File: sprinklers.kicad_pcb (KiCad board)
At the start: 2 copper layers, 128.7 x 88 mm, 43 parts, among them K1 SANYOU_SRD_Form_C, K2 SANYOU_SRD_Form_C, K3 SANYOU_SRD_Form_C, K4 SANYOU_SRD_Form_C, K5 SANYOU_SRD_Form_C, K6 SANYOU_SRD_Form_C, Q1 Q_NMOS_GDS, Q2 Q_NMOS_GDS, Q3 Q_NMOS_GDS, Q4 Q_NMOS_GDS, Q5 Q_NMOS_GDS, Q6 Q_NMOS_GDS, U1 LM2596S-5, U2 ESP32-WROOM-32D, U3 AP1117-33

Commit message: orgenize schematic
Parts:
- added 26 27 28 29: PinHeader_1x04_P2.54mm_Vertical, Connector_PinHeader_2.54mm:PinHeader_1x04_P2.54mm_Vertical, F.Cu at (145.0, 56.9)
- GND 5V 3V3: renamed from DC OUT
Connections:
- C5 pad 1: AC -> Net-(D4-K)
- D4 pad 1: AC -> Net-(D4-K)
- U1 pad 1: AC -> Net-(D4-K)
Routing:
- net AC: track 165.7 -> 127.0 mm
- net Net-(D4-K): track 0.00 -> 38.0 mm
- net unconnected-(U2-IO5-Pad29): track 0.00 -> 7.18 mm
- net unconnected-(U2-IO17-Pad28): track 0.00 -> 6.66 mm
- net unconnected-(U2-IO4-Pad26): track 0.00 -> 6.52 mm
- net unconnected-(U2-IO16-Pad27): track 0.00 -> 6.13 mm
- net unconnected-(U2-IO0-Pad25): track 30.5 -> 33.2 mm
- net unconnected-(U2-TXD0/IO1-Pad35): track 11.8 -> 9.62 mm
- net Net-(U1-FB): track 202.3 -> 203.0 mm, vias 4 -> 3
- net unconnected-(U2-EN-Pad3): track 36.6 -> 36.0 mm

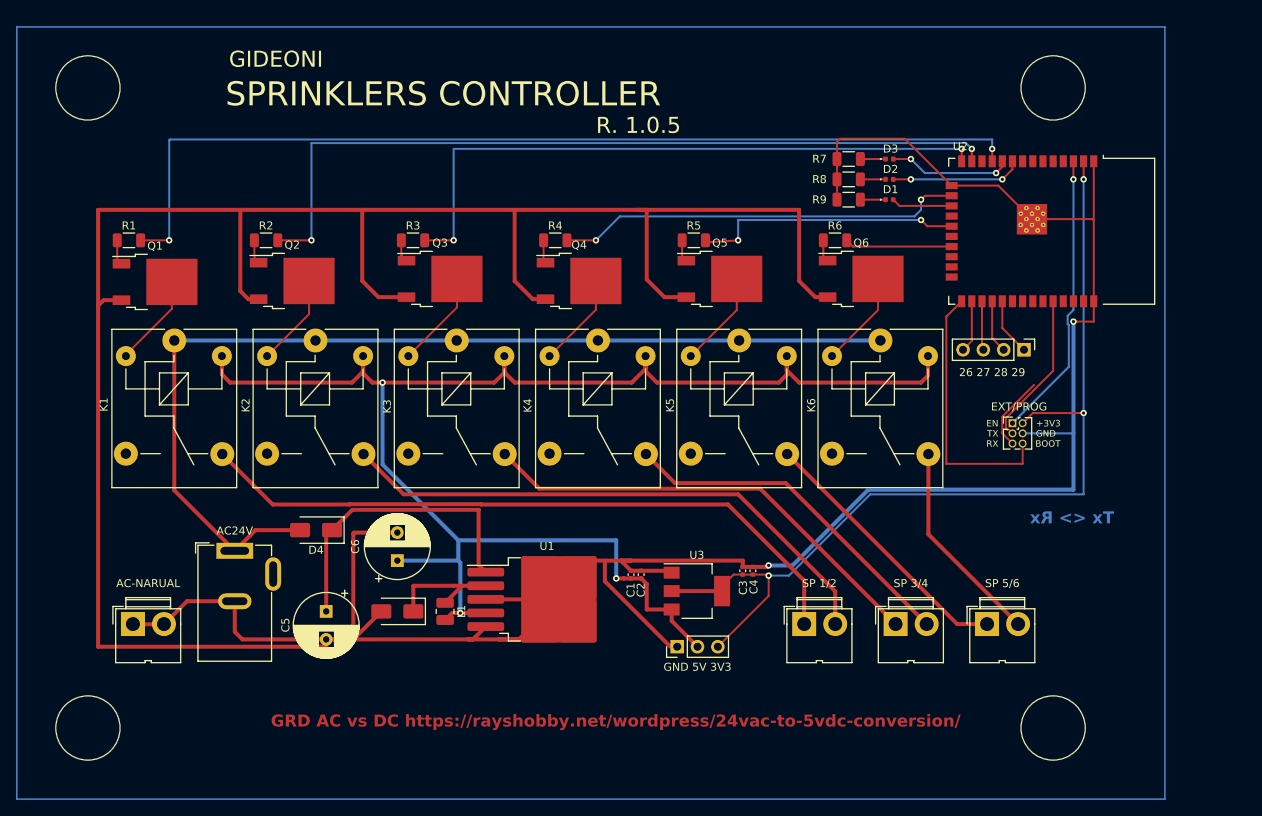
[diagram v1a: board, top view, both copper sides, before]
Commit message: Replacing inductor
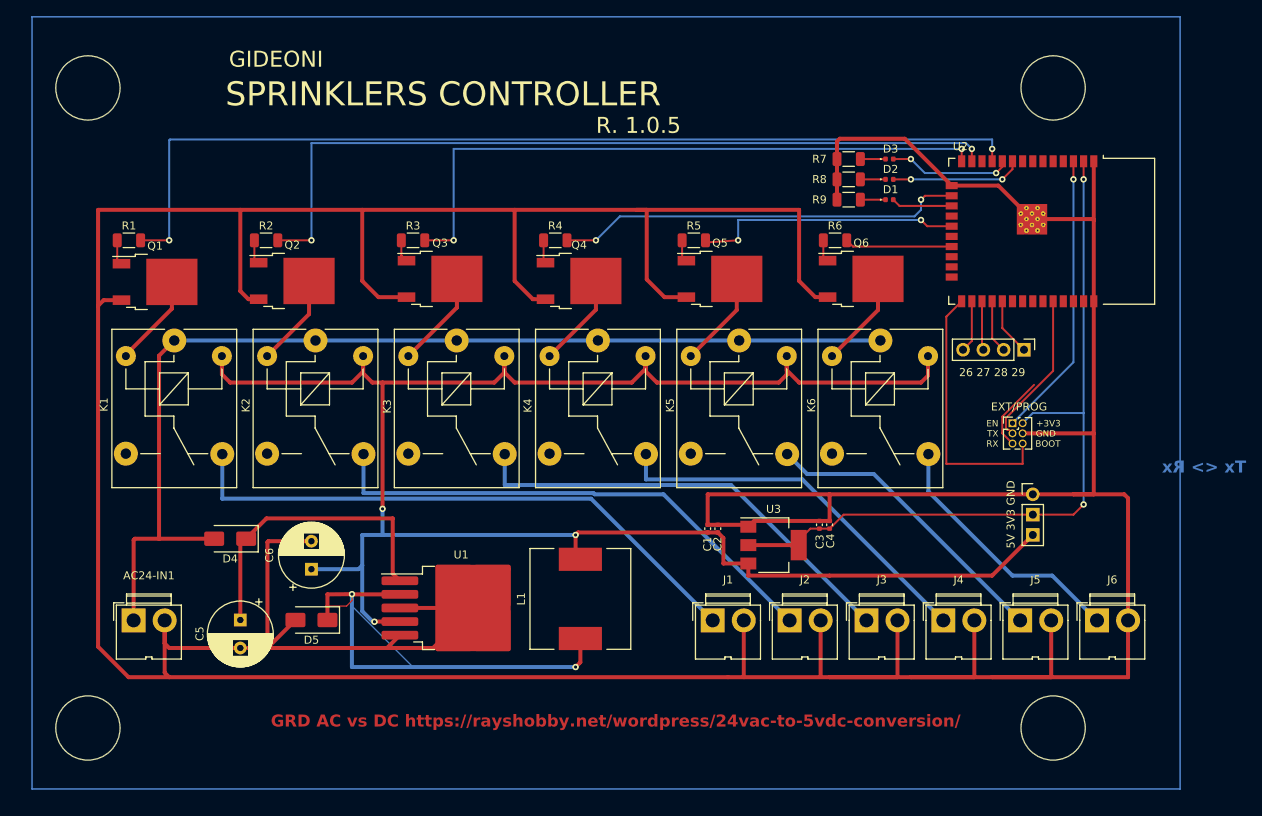
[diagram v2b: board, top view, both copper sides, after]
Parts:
- removed AC-NARUAL: JWT_A3963_1x02_P3.96mm_Vertical, Connector:JWT_A3963_1x02_P3.96mm_Vertical
- removed AC24V: Conn_Coaxial_Power, Connector_BarrelJack:BarrelJack_GCT_DCJ200-10-A_Horizontal
- removed SP 1/2: JWT_A3963_1x02_P3.96mm_Vertical, Connector:JWT_A3963_1x02_P3.96mm_Vertical
- removed SP 3/4: JWT_A3963_1x02_P3.96mm_Vertical, Connector:JWT_A3963_1x02_P3.96mm_Vertical
- removed SP 5/6: JWT_A3963_1x02_P3.96mm_Vertical, Connector:JWT_A3963_1x02_P3.96mm_Vertical
- added AC24-IN1: Conn_01x02, Connector:JWT_A3963_1x02_P3.96mm_Vertical, F.Cu at (33.7, 90.7)
- added J1: Conn_01x02, Connector:JWT_A3963_1x02_P3.96mm_Vertical, F.Cu at (106.0, 90.7)
- added J2: Conn_01x02, Connector:JWT_A3963_1x02_P3.96mm_Vertical, F.Cu at (115.6, 90.7)
- added J3: Conn_01x02, Connector:JWT_A3963_1x02_P3.96mm_Vertical, F.Cu at (125.3, 90.7)
- added J4: Conn_01x02, Connector:JWT_A3963_1x02_P3.96mm_Vertical, F.Cu at (134.9, 90.7)
- added J5: Conn_01x02, Connector:JWT_A3963_1x02_P3.96mm_Vertical, F.Cu at (144.5, 90.7)
- added J6: Conn_01x02, Connector:JWT_A3963_1x02_P3.96mm_Vertical, F.Cu at (154.1, 90.7)
- 5V 3V3 GND: renamed from GND 5V 3V3
- L1: footprint Inductor_SMD:L_1008_2520Metric -> Inductor_SMD:L_12x12mm_H8mm
- moved 5V 3V3 GND 48.4 mm to (146.1, 74.9), turned to 0 degrees
- moved L1 17.0 mm to (89.5, 88.0), turned to 90 degrees
- moved C2 11.2 mm to (106.7, 79.2)
- moved C4 11.2 mm to (120.7, 78.7)
- moved C1 11.2 mm to (105.4, 79.2)
- moved C3 11.2 mm to (119.4, 78.7)
- moved U3 11.2 mm to (113.6, 81.3)
- moved C5 10.8 mm to (47.0, 90.6)
- moved D4 10.8 mm to (45.7, 80.5)
- moved U1 10.8 mm to (74.6, 89.1)
- moved C6 10.8 mm to (55.9, 84.3)
- moved D5 10.8 mm to (55.9, 90.6)
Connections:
- net AC renamed Net-(AC24-IN1-Pin_1)
- 5V 3V3 GND pad 2: Net-(U1-FB) -> Net-(U2-VDD)
- 5V 3V3 GND pad 3: Net-(U2-VDD) -> Net-(U1-FB)
- K1 pad 4: unconnected-(K1-Pad4) -> Net-(J1-Pin_1)
- K2 pad 4: unconnected-(K2-Pad4) -> Net-(J2-Pin_1)
- K3 pad 4: unconnected-(K3-Pad4) -> Net-(J3-Pin_1)
- K4 pad 4: unconnected-(K4-Pad4) -> Net-(J4-Pin_1)
- K5 pad 4: unconnected-(K5-Pad4) -> Net-(J5-Pin_1)
- K6 pad 4: unconnected-(K6-Pad4) -> Net-(J6-Pin_1)
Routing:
- net GND1: track 537.7 -> 699.6 mm, vias 2 -> 0
- net unconnected-(K1-Pad4): track 84.7 -> 0.00 mm
- net Net-(J1-Pin_1): track 0.00 -> 73.3 mm
- net unconnected-(K2-Pad4): track 70.2 -> 0.00 mm
- net Net-(J2-Pin_1): track 0.00 -> 64.7 mm
- net unconnected-(K3-Pad4): track 57.7 -> 0.00 mm
- net Net-(J3-Pin_1): track 0.00 -> 56.1 mm
- net Net-(D5-K): track 18.2 -> 68.8 mm, vias 0 -> 2
- net Net-(U1-FB): track 203.0 -> 250.9 mm
- net Net-(J4-Pin_1): track 0.00 -> 47.6 mm
- net unconnected-(K4-Pad4): track 43.9 -> 0.00 mm
- net Net-(J5-Pin_1): track 0.00 -> 37.7 mm
- net unconnected-(K5-Pad4): track 33.8 -> 0.00 mm
- net Net-(J6-Pin_1): track 0.00 -> 32.4 mm
- net unconnected-(K6-Pad4): track 25.9 -> 0.00 mm
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
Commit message: tx/rx fix
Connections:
- EXT/PROG pad 3: unconnected-(U2-RXD0/IO3-Pad34) -> unconnected-(U2-TXD0/IO1-Pad35)
- EXT/PROG pad 5: unconnected-(U2-TXD0/IO1-Pad35) -> unconnected-(U2-RXD0/IO3-Pad34)
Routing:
- net unconnected-(U2-TXD0/IO1-Pad35): track 9.62 -> 19.9 mm
- net GND1: track 699.6 -> 707.8 mm
- net Net-(U1-FB): track 250.9 -> 257.6 mm
- net Net-(AC24-IN1-Pin_1): track 134.0 -> 138.5 mm
- net Net-(J1-Pin_1): track 73.3 -> 75.2 mm
- net Net-(U2-IO13): track 51.1 -> 52.9 mm
- net unconnected-(U2-RXD0/IO3-Pad34): track 19.4 -> 21.0 mm
- net Net-(J2-Pin_1): track 64.7 -> 66.3 mm
- net Net-(J3-Pin_1): track 56.1 -> 57.5 mm
- net Net-(J4-Pin_1): track 47.6 -> 48.7 mm

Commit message: fix nets
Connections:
- net Net-(U1-FB) renamed DC5V
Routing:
- net Net-(D5-K): track 68.8 -> 64.6 mm
- net DC5V: track 257.6 -> 254.9 mm, vias 3 -> 2
- net Net-(D4-K): track 38.0 -> 39.2 mm
- net Net-(U2-VDD): track 95.7 -> 95.1 mm
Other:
- board text removed: "Tx <> Rx"

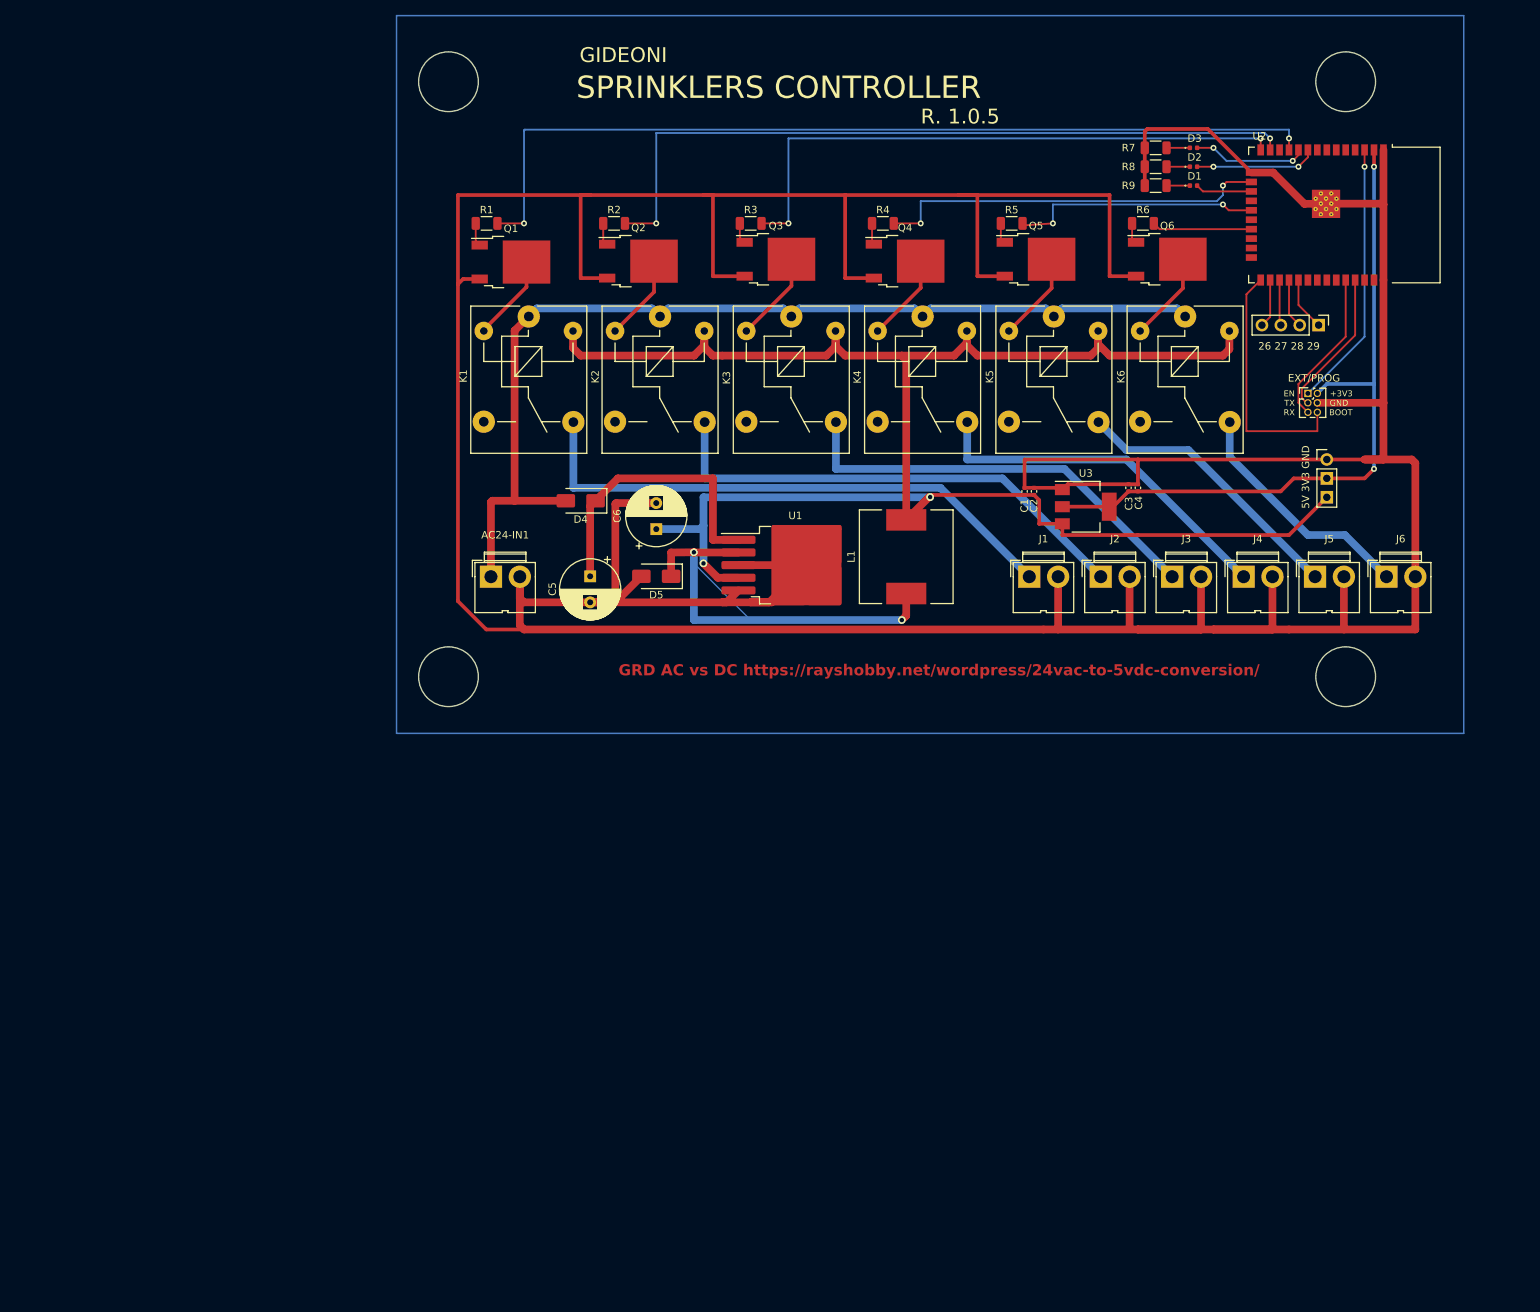
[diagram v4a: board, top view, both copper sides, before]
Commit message: add moisture sensor
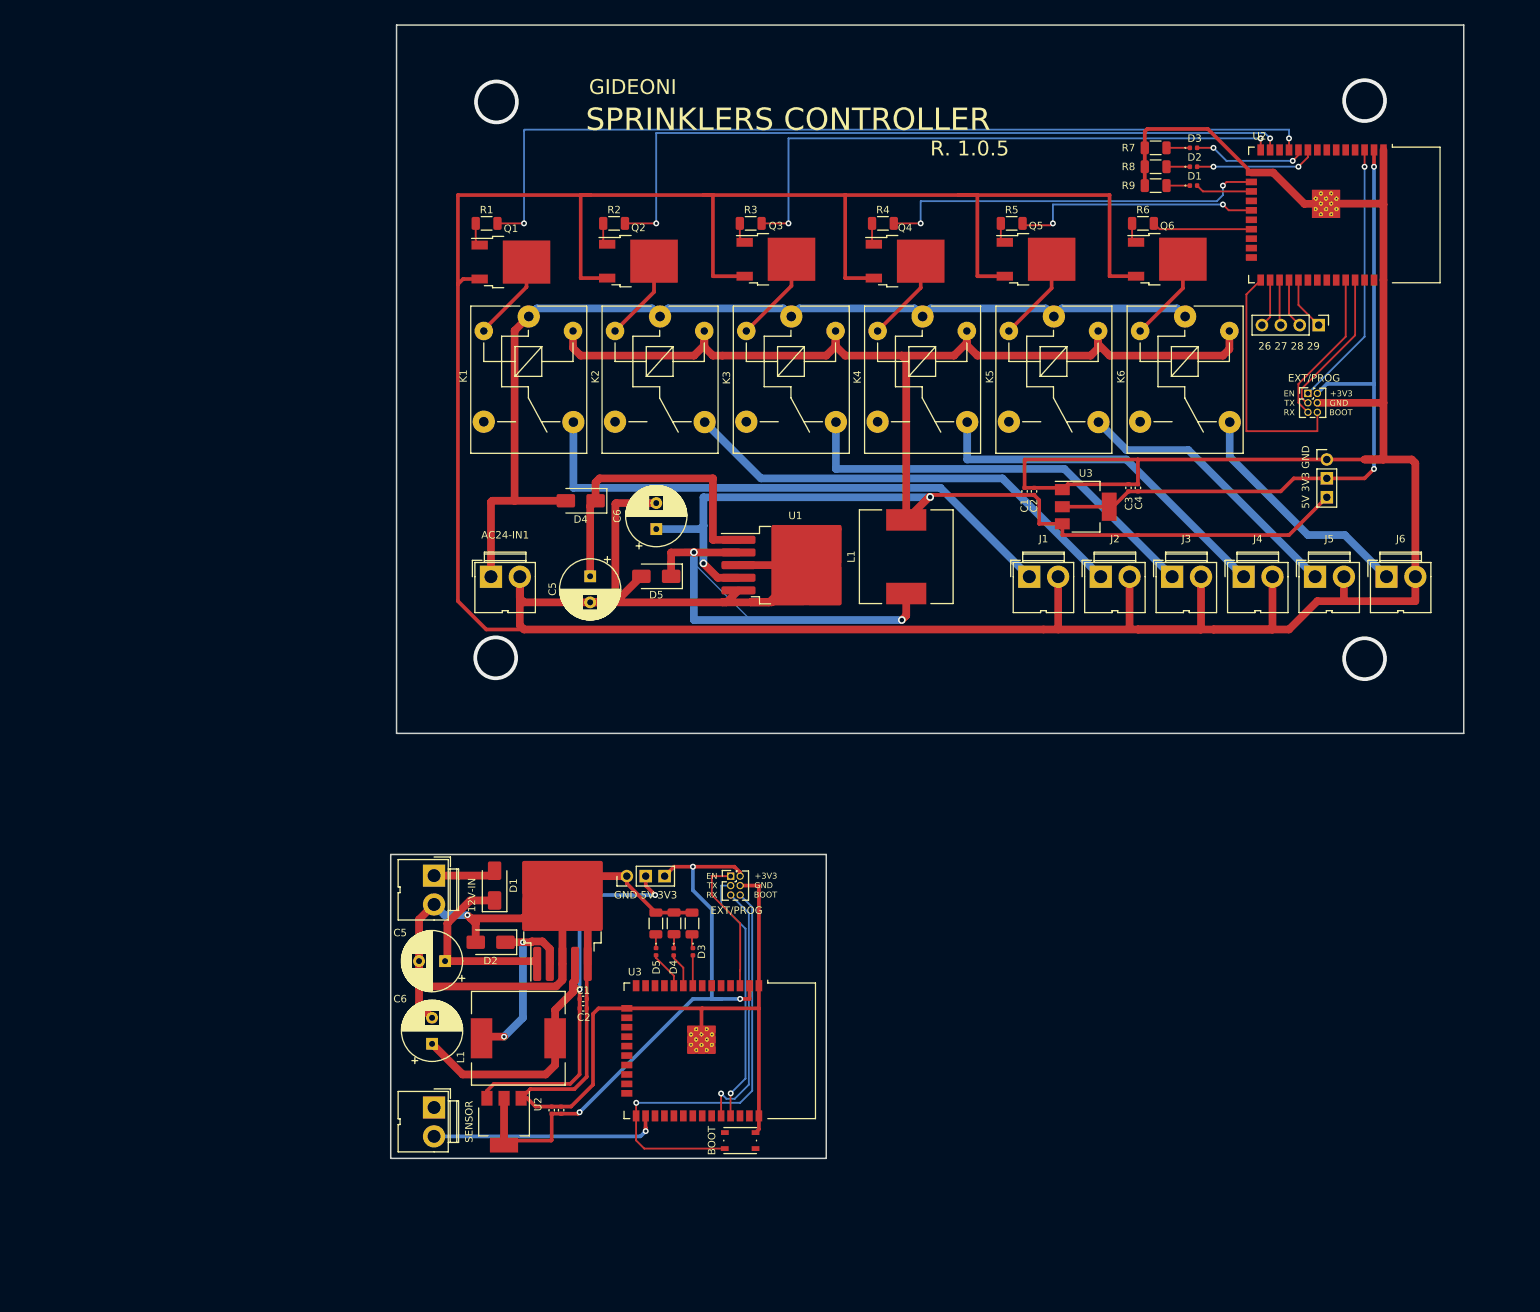
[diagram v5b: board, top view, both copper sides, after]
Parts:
- added 12V-IN: Conn_01x02, Connector:JWT_A3963_1x02_P3.96mm_Vertical, F.Cu at (26.0, 130.9)
- added BOOT: SW_SPST, Button_Switch_SMD:SW_Push_1P1T_NO_Vertical_Wuerth_434133025816, F.Cu at (67.2, 166.5)
- added C1: 10uF, Capacitor_SMD:C_0402_1005Metric, F.Cu at (46.0, 147.5)
- added C2: 100nF, Capacitor_SMD:C_0402_1005Metric, F.Cu at (46.0, 148.7)
- added C3: 10uF, Capacitor_SMD:C_0402_1005Metric, F.Cu at (41.8, 162.4)
- added C4: 100nF, Capacitor_SMD:C_0402_1005Metric, F.Cu at (43.1, 162.4)
- added C5: C_Polarized, Capacitor_THT:CP_Radial_D8.0mm_P3.50mm, F.Cu at (27.5, 142.4)
- added C6: C_Polarized, Capacitor_THT:CP_Radial_D8.0mm_P3.50mm, F.Cu at (25.7, 153.5)
- added D1: US1A, Diode_SMD:D_SMA, F.Cu at (34.1, 132.2)
- added D2: B140-E3, Diode_SMD:D_SMA, F.Cu at (33.6, 139.8)
- added D3: LED, LED_SMD:LED_0402_1005Metric, F.Cu at (60.8, 141.1)
- added D4: LED, LED_SMD:LED_0402_1005Metric, F.Cu at (58.2, 141.1)
- added D5: LED, LED_SMD:LED_0402_1005Metric, F.Cu at (55.9, 141.1)
- added EXT/PROG: PinHeader_2x03_P1.27mm_Vertical, Connector_PinHeader_1.27mm:PinHeader_2x03_P1.27mm_Vertical, F.Cu at (65.9, 131.0)
- added GND 5V 3V3: PinHeader_1x03_P2.54mm_Vertical, Connector_PinHeader_2.54mm:PinHeader_1x03_P2.54mm_Vertical, F.Cu at (51.9, 131.0)
- added L1: L, Inductor_SMD:L_12x12mm_H8mm, F.Cu at (37.3, 152.8)
- added R1: 130, Resistor_SMD:R_1206_3216Metric, F.Cu at (60.7, 137.3)
- added R2: 130, Resistor_SMD:R_1206_3216Metric, F.Cu at (58.3, 137.3)
- added R3: 130, Resistor_SMD:R_1206_3216Metric, F.Cu at (55.8, 137.3)
- added SENSOR: Conn_01x02, Connector:JWT_A3963_1x02_P3.96mm_Vertical, F.Cu at (26.0, 162.1)
- added U1: LM2596S-5, Package_TO_SOT_SMD:TO-263-5_TabPin3, F.Cu at (43.3, 135.1)
- added U2: AP1117-33, Package_TO_SOT_SMD:SOT-223-3_TabPin2, F.Cu at (35.4, 164.0)
- added U3: ESP32-WROOM-32D, RF_Module:ESP32-WROOM-32D, F.Cu at (61.4, 154.4)
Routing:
- net (no net): track 0.00 -> 358.7 mm, vias 0 -> 13
- net GND1: track 707.8 -> 896.5 mm, vias 0 -> 1
- net Net-(D1-K): track 3.14 -> 28.5 mm
- net Net-(D2-K): track 3.14 -> 28.5 mm, vias 0 -> 2
- net Net-(AC24-IN1-Pin_1): track 138.5 -> 146.9 mm
- net Net-(J2-Pin_1): track 66.3 -> 61.9 mm
- net Net-(D3-A): track 15.4 -> 19.5 mm
- net Net-(D4-K): track 39.2 -> 42.5 mm
- net Net-(D3-K): track 3.14 -> 5.04 mm
- net Net-(D5-K): track 64.6 -> 66.5 mm
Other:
- board size 128.7 x 88 mm -> 144.3 x 152.4 mm
- board text added: "MOISTURE SENSOR"
